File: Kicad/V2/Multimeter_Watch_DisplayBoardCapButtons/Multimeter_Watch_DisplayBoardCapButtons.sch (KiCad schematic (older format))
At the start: 24 parts, among them J1 51281-1294, J2 Conn_01x11_Female, J3 Conn_01x11_Female, U1 AT42QT1070-S

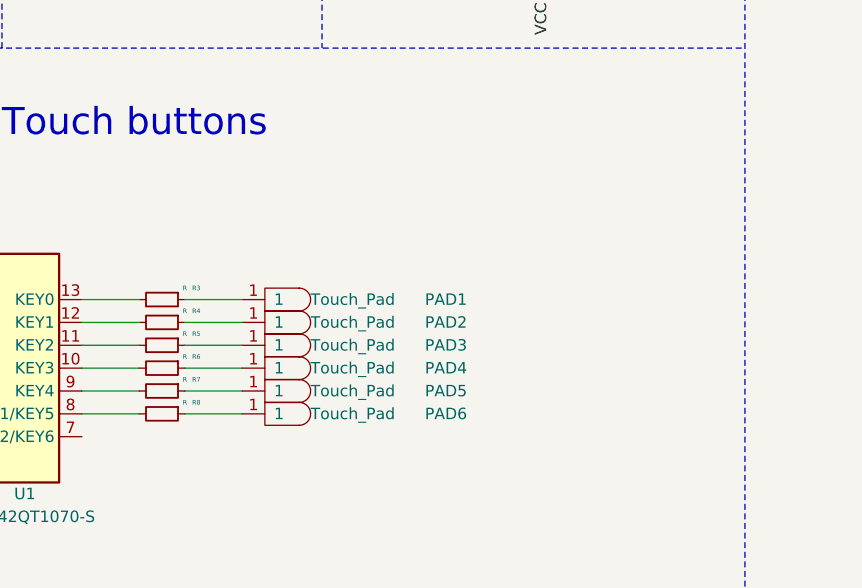
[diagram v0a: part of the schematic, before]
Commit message: top board capacitance buttons
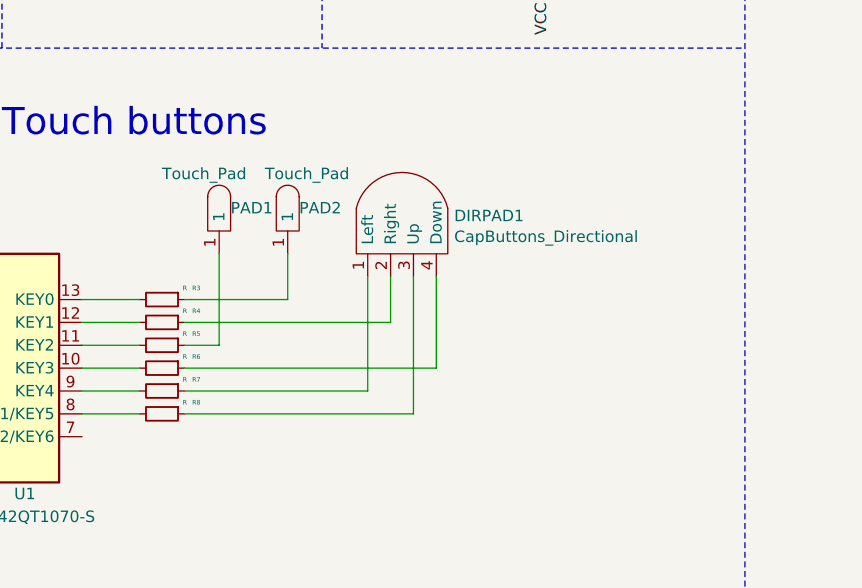
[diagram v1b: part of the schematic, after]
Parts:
- removed PAD3, PAD4, PAD5, PAD6: Touch_Pad, symbol Multimeter_Watch_Custom_Symbols:Touch_Pad
- added DIRPAD1: CapButtons_Directional, Multimeter_Watch_Custom_Footprints:CapButtons_Directional, symbol Multimeter_Watch_Custom_Symbols:CapButtons_Directional
- PAD1: footprint (none) -> Multimeter_Watch_Custom_Footprints:CapButton_Left
- PAD2: footprint (none) -> Multimeter_Watch_Custom_Footprints:CapButton_Right
- R1, R2, R3, R4, R5, R6, R7, R8: footprint Resistor_SMD:R_0815_2038Metric_Pad1.53x4.00mm_HandSolder -> Resistor_SMD:R_0805_2012Metric_Pad1.15x1.40mm_HandSolder
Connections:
- net at PAD1.1: now also R5.1; no longer R3.1
- net at R4.1: now also DIRPAD1.2 (Right); no longer PAD2.1
- net at R6.1: now also DIRPAD1.4 (Down)
- net at R7.1: now also DIRPAD1.1 (Left)
- net at R8.1: now also DIRPAD1.3 (Up)
- new net: PAD2.1, R3.1
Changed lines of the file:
@@
 F 0 "R1" H 1550 3000 50  0000 R CNN
 F 1 "R" H 1500 3100 50  0000 R CNN
-F 2 "Resistor_SMD:R_0815_2038Metric_Pad1.53x4.00mm_HandSolder" V 1330 3050 50  0001 C CNN
+F 2 "Resistor_SMD:R_0805_2012Metric_Pad1.15x1.40mm_HandSolder" V 1330 3050 50  0001 C CNN
 F 3 "~" H 1400 3050 50  0001 C CNN
 	1    1400 3050
@@
 F 0 "R2" H 1570 3096 50  0000 L CNN
 F 1 "R" H 1570 3005 50  0000 L CNN
-F 2 "Resistor_SMD:R_0815_2038Metric_Pad1.53x4.00mm_HandSolder" V 1430 3050 50  0001 C CNN
+F 2 "Resistor_SMD:R_0805_2012Metric_Pad1.15x1.40mm_HandSolder" V 1430 3050 50  0001 C CNN
 F 3 "~" H 1500 3050 50  0001 C CNN
 	1    1500 3050
@@
 F 0 "R3" V 3400 3200 20  0000 C CNN
 F 1 "R" V 3400 3150 20  0000 C CNN
-F 2 "Resistor_SMD:R_0815_2038Metric_Pad1.53x4.00mm_HandSolder" H 3450 3050 50  0001 C CNN
+F 2 "Resistor_SMD:R_0805_2012Metric_Pad1.15x1.40mm_HandSolder" H 3450 3050 50  0001 C CNN
 F 3 "~" H 3450 3050 50  0001 C CNN
 	1    3450 3050
@@
 F 0 "R4" V 3400 3300 20  0000 C CNN
 F 1 "R" V 3400 3250 20  0000 C CNN
-F 2 "Resistor_SMD:R_0815_2038Metric_Pad1.53x4.00mm_HandSolder" H 3450 3150 50  0001 C CNN
+F 2 "Resistor_SMD:R_0805_2012Metric_Pad1.15x1.40mm_HandSolder" H 3450 3150 50  0001 C CNN
 F 3 "~" H 3450 3150 50  0001 C CNN
 	1    3450 3150
@@
 F 0 "R5" V 3400 3400 20  0000 C CNN
 F 1 "R" V 3400 3350 20  0000 C CNN
-F 2 "Resistor_SMD:R_0815_2038Metric_Pad1.53x4.00mm_HandSolder" H 3450 3250 50  0001 C CNN
+F 2 "Resistor_SMD:R_0805_2012Metric_Pad1.15x1.40mm_HandSolder" H 3450 3250 50  0001 C CNN
 F 3 "~" H 3450 3250 50  0001 C CNN
 	1    3450 3250
@@
 F 0 "R6" V 3400 3500 20  0000 C CNN
 F 1 "R" V 3400 3450 20  0000 C CNN
-F 2 "Resistor_SMD:R_0815_2038Metric_Pad1.53x4.00mm_HandSolder" H 3450 3350 50  0001 C CNN
+F 2 "Resistor_SMD:R_0805_2012Metric_Pad1.15x1.40mm_HandSolder" H 3450 3350 50  0001 C CNN
 F 3 "~" H 3450 3350 50  0001 C CNN
 	1    3450 3350
@@
 F 0 "R7" V 3400 3600 20  0000 C CNN
 F 1 "R" V 3400 3550 20  0000 C CNN
-F 2 "Resistor_SMD:R_0815_2038Metric_Pad1.53x4.00mm_HandSolder" H 3450 3450 50  0001 C CNN
+F 2 "Resistor_SMD:R_0805_2012Metric_Pad1.15x1.40mm_HandSolder" H 3450 3450 50  0001 C CNN
 F 3 "~" H 3450 3450 50  0001 C CNN
 	1    3450 3450
@@
 F 0 "R8" V 3400 3700 20  0000 C CNN
 F 1 "R" V 3400 3650 20  0000 C CNN
-F 2 "Resistor_SMD:R_0815_2038Metric_Pad1.53x4.00mm_HandSolder" H 3450 3550 50  0001 C CNN
+F 2 "Resistor_SMD:R_0805_2012Metric_Pad1.15x1.40mm_HandSolder" H 3450 3550 50  0001 C CNN
 F 3 "~" H 3450 3550 50  0001 C CNN
 	1    3450 3550
@@
 Wire Wire Line
 	3100 3550 3350 3550
-$Comp
-L Multimeter_Watch_Custom_Symbols:Touch_Pad PAD1
-U 1 1 5F771E09
-P 4000 3050
-F 0 "PAD1" H 4600 3050 50  0000 L CNN
-F 1 "Touch_Pad" H 4100 3050 50  0000 L CNN
-F 2 "" H 4000 3050 50  0001 C CNN
-F 3 "" H 4000 3050 50  0001 C CNN
-	1    4000 3050
-	1    0    0    -1
-$EndComp
-$Comp
-L Multimeter_Watch_Custom_Symbols:Touch_Pad PAD2
-U 1 1 5F77251C
-P 4000 3150
-F 0 "PAD2" H 4600 3150 50  0000 L CNN
-F 1 "Touch_Pad" H 4100 3150 50  0000 L CNN
-F 2 "" H 4000 3150 50  0001 C CNN
-F 3 "" H 4000 3150 50  0001 C CNN
-	1    4000 3150
-	1    0    0    -1
-$EndComp
-$Comp
-L Multimeter_Watch_Custom_Symbols:Touch_Pad PAD3
-U 1 1 5F772D1C
-P 4000 3250
-F 0 "PAD3" H 4600 3250 50  0000 L CNN
-F 1 "Touch_Pad" H 4100 3250 50  0000 L CNN
-F 2 "" H 4000 3250 50  0001 C CNN
-F 3 "" H 4000 3250 50  0001 C CNN
-	1    4000 3250
-	1    0    0    -1
-$EndComp
-$Comp
-L Multimeter_Watch_Custom_Symbols:Touch_Pad PAD4
-U 1 1 5F772D26
-P 4000 3350
-F 0 "PAD4" H 4600 3350 50  0000 L CNN
-F 1 "Touch_Pad" H 4100 3350 50  0000 L CNN
-F 2 "" H 4000 3350 50  0001 C CNN
-F 3 "" H 4000 3350 50  0001 C CNN
-	1    4000 3350
-	1    0    0    -1
-$EndComp
-$Comp
-L Multimeter_Watch_Custom_Symbols:Touch_Pad PAD5
-U 1 1 5F773797
-P 4000 3450
-F 0 "PAD5" H 4600 3450 50  0000 L CNN
-F 1 "Touch_Pad" H 4100 3450 50  0000 L CNN
-F 2 "" H 4000 3450 50  0001 C CNN
-F 3 "" H 4000 3450 50  0001 C CNN
-	1    4000 3450
-	1    0    0    -1
-$EndComp
-$Comp
-L Multimeter_Watch_Custom_Symbols:Touch_Pad PAD6
-U 1 1 5F7737A1
-P 4000 3550
-F 0 "PAD6" H 4600 3550 50  0000 L CNN
-F 1 "Touch_Pad" H 4100 3550 50  0000 L CNN
-F 2 "" H 4000 3550 50  0001 C CNN
-F 3 "" H 4000 3550 50  0001 C CNN
-	1    4000 3550
-	1    0    0    -1
-$EndComp
-Wire Wire Line
-	3800 3050 3550 3050
-Wire Wire Line
-	3550 3150 3800 3150
-Wire Wire Line
-	3800 3250 3550 3250
-Wire Wire Line
-	3550 3350 3800 3350
-Wire Wire Line
-	3800 3450 3550 3450
-Wire Wire Line
-	3550 3550 3800 3550
 Text Notes 2750 2350 0    118  ~ 0
 Touch buttons
@@
 Wire Notes Line
 	6000 500  6000 4500
+$Comp
+L Multimeter_Watch_Custom_Symbols:CapButtons_Directional DIRPAD1
+U 1 1 5F7511E5
+P 4350 2750
+F 0 "DIRPAD1" V 4416 2372 50  0000 R CNN
+F 1 "CapButtons_Directional" V 4325 2372 50  0000 R CNN
+F 2 "Multimeter_Watch_Custom_Footprints:CapButtons_Directional" H 4350 3000 50  0001 C CNN
+F 3 "" H 4350 3000 50  0001 C CNN
+	1    4350 2750
+	0    -1   -1   0
+$EndComp
+$Comp
+L Multimeter_Watch_Custom_Symbols:Touch_Pad PAD1
+U 1 1 5F751E9A
+P 3700 2650
+F 0 "PAD1" V 3700 2600 50  0000 R CNN
+F 1 "Touch_Pad" V 3850 2900 50  0000 R CNN
+F 2 "Multimeter_Watch_Custom_Footprints:CapButton_Left" H 3700 2650 50  0001 C CNN
+F 3 "" H 3700 2650 50  0001 C CNN
+	1    3700 2650
+	0    -1   -1   0
+$EndComp
+$Comp
+L Multimeter_Watch_Custom_Symbols:Touch_Pad PAD2
+U 1 1 5F752AB3
+P 4000 2650
+F 0 "PAD2" V 4000 2600 50  0000 R CNN
+F 1 "Touch_Pad" V 4150 2750 50  0000 R CNN
+F 2 "Multimeter_Watch_Custom_Footprints:CapButton_Right" H 4000 2650 50  0001 C CNN
+F 3 "" H 4000 2650 50  0001 C CNN
+	1    4000 2650
+	0    -1   -1   0
+$EndComp
+Wire Wire Line
+	3550 3250 3700 3250
+Wire Wire Line
+	3700 3250 3700 2850
+Wire Wire Line
+	4650 3350 4650 2950
+Wire Wire Line
+	3550 3350 4650 3350
+Wire Wire Line
+	4350 3450 4350 2950
+Wire Wire Line
+	3550 3450 4350 3450
+Wire Wire Line
+	4550 3550 4550 2950
+Wire Wire Line
+	3550 3550 4550 3550
+Wire Wire Line
+	4450 3150 4450 2950
+Wire Wire Line
+	3550 3150 4450 3150
+Wire Wire Line
+	4000 2850 4000 3050
+Wire Wire Line
+	3550 3050 4000 3050
 $EndSCHEMATC

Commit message: fix flex conn
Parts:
- PAD1, PAD2: symbol Multimeter_Watch_Custom_Symbols:Touch_Pad -> Multimeter_Watch_DisplayBoardCapButtons-rescue:Touch_Pad-Multimeter_Watch_Custom_Symbols
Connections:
- net GND: now also J1.3, J1.4; no longer J1.10, J1.9
- net PB5: now also J1.7; no longer J1.6
- net PB6: now also J1.9; no longer J1.4
- net PB7: now also J1.8; no longer J1.5
- net PD5: now also J1.6; no longer J1.7
- net PD6: now also J1.5; no longer J1.8
- net PE4: now also J1.11; no longer J1.2
- net PE5: now also J1.10; no longer J1.3
- net SCL: now also J1.2; no longer J1.11
- net SDA: now also J1.1; no longer J1.12
- net VCC: now also J1.12; no longer J1.1
- net at R5.1: now also PAD1.~; no longer PAD1.1
- net at R3.1: now also PAD2.~; no longer PAD2.1
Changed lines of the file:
@@
 Text Label 6300 900  1    47   ~ 0
 PD6
-Text Label 4850 1450 3    47   ~ 0
+Text Label 4950 1450 3    47   ~ 0
 PB5
+Text Label 5350 1450 3    50   ~ 0
+PE4
 Text Label 4450 1450 3    50   ~ 0
-PE4
-Text Label 5350 1450 3    50   ~ 0
 SCL
-Text Label 5450 1450 3    50   ~ 0
+Text Label 4350 1450 3    50   ~ 0
 SDA
-Text Label 4550 1450 3    50   ~ 0
+Text Label 5250 1450 3    50   ~ 0
 PE5
 Text Label 5150 1750 3    50   ~ 0
 VCC
+Text Label 5050 1450 3    50   ~ 0
+PB7
+Text Label 5150 1450 3    50   ~ 0
+PB6
+Text Label 4550 1450 3    50   ~ 0
+GND
+Text Label 4850 1450 3    50   ~ 0
+PD5
 Text Label 4750 1450 3    50   ~ 0
-PB7
-Text Label 4650 1450 3    50   ~ 0
-PB6
-Text Label 5250 1450 3    50   ~ 0
-GND
-Text Label 4950 1450 3    50   ~ 0
-PD5
-Text Label 5050 1450 3    50   ~ 0
 PD6
 $Comp
@@
 	1    0    0    -1
 $EndComp
-Text Label 5150 1450 3    50   ~ 0
+Text Label 4650 1450 3    50   ~ 0
 GND
 Wire Wire Line
@@
 Wire Wire Line
 	9750 2000 9750 2100
-Text Label 4350 1450 3    50   ~ 0
+Text Label 5450 1450 3    50   ~ 0
 VCC
 Wire Notes Line
@@
 $EndComp
 $Comp
-L Multimeter_Watch_Custom_Symbols:Touch_Pad PAD1
+L Multimeter_Watch_DisplayBoardCapButtons-rescue:Touch_Pad-Multimeter_Watch_Custom_Symbols PAD1
 U 1 1 5F751E9A
 P 3700 2650
@@
 $EndComp
 $Comp
-L Multimeter_Watch_Custom_Symbols:Touch_Pad PAD2
+L Multimeter_Watch_DisplayBoardCapButtons-rescue:Touch_Pad-Multimeter_Watch_Custom_Symbols PAD2
 U 1 1 5F752AB3
 P 4000 2650

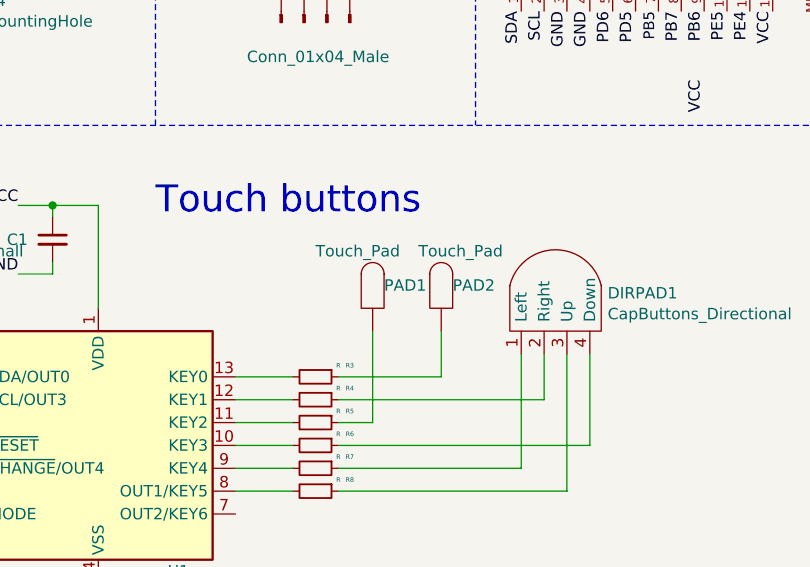
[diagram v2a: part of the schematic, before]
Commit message: drc update and fixes to capbuttons board
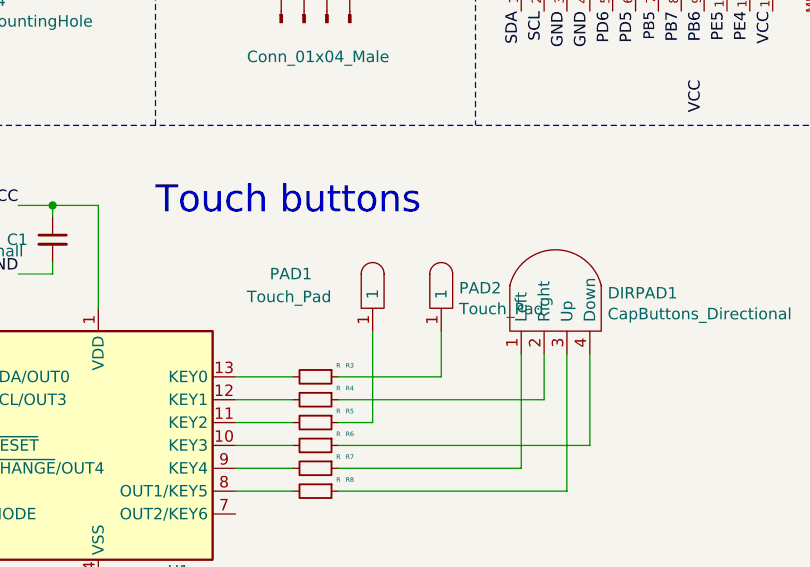
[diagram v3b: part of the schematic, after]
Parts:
- removed PAD1: Touch_Pad, Multimeter_Watch_Custom_Footprints:CapButton_Left, symbol Multimeter_Watch_DisplayBoardCapButtons-rescue:Touch_Pad-Multimeter_Watch_Custo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
- removed PAD2: Touch_Pad, Multimeter_Watch_Custom_Footprints:CapButton_Right, symbol Multimeter_Watch_DisplayBoardCapButtons-rescue:Touch_Pad-Multimeter_Watch_Custo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
- added PAD1: Touch_Pad, Multimeter_Watch_Custom_Footprints:CapButton_Left, symbol Multimeter_Watch_Custom_Symbols:Touch_Pad
- added PAD2: Touch_Pad, Multimeter_Watch_Custom_Footprints:CapButton_Right, symbol Multimeter_Watch_Custom_Symbols:Touch_Pad
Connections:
- net at R5.1: now also PAD1.1
- net at R3.1: now also PAD2.1
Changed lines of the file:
@@
-	0    -1   -1   0
-$EndComp
-$Comp
-L Multimeter_Watch_DisplayBoardCapButtons-rescue:Touch_Pad-Multimeter_Watch_Custom_Symbols PAD1
-U 1 1 5F751E9A
-P 3700 2650
-F 0 "PAD1" V 3700 2600 50  0000 R CNN
-F 1 "Touch_Pad" V 3850 2900 50  0000 R CNN
-F 2 "Multimeter_Watch_Custom_Footprints:CapButton_Left" H 3700 2650 50  0001 C CNN
-F 3 "" H 3700 2650 50  0001 C CNN
-	1    3700 2650
-	0    -1   -1   0
-$EndComp
-$Comp
-L Multimeter_Watch_DisplayBoardCapButtons-rescue:Touch_Pad-Multimeter_Watch_Custom_Symbols PAD2
-U 1 1 5F752AB3
-P 4000 2650
-F 0 "PAD2" V 4000 2600 50  0000 R CNN
-F 1 "Touch_Pad" V 4150 2750 50  0000 R CNN
-F 2 "Multimeter_Watch_Custom_Footprints:CapButton_Right" H 4000 2650 50  0001 C CNN
-F 3 "" H 4000 2650 50  0001 C CNN
-	1    4000 2650
 	0    -1   -1   0
 $EndComp
@@
 Wire Wire Line
 	3550 3050 4000 3050
+$Comp
+L Multimeter_Watch_Custom_Symbols:Touch_Pad PAD1
+U 1 1 5F9B02FC
+P 3700 2650
+F 0 "PAD1" V 3750 3100 50  0000 R CNN
+F 1 "Touch_Pad" V 3650 3200 50  0000 R CNN
+F 2 "Multimeter_Watch_Custom_Footprints:CapButton_Left" H 3700 2650 50  0001 C CNN
+F 3 "" H 3700 2650 50  0001 C CNN
+	1    3700 2650
+	0    -1   -1   0
+$EndComp
+$Comp
+L Multimeter_Watch_Custom_Symbols:Touch_Pad PAD2
+U 1 1 5F9B0B06
+P 4000 2650
+F 0 "PAD2" V 3988 2572 50  0000 R CNN
+F 1 "Touch_Pad" V 3897 2572 50  0000 R CNN
+F 2 "Multimeter_Watch_Custom_Footprints:CapButton_Right" H 4000 2650 50  0001 C CNN
+F 3 "" H 4000 2650 50  0001 C CNN
+	1    4000 2650
+	0    -1   -1   0
+$EndComp
 $EndSCHEMATC
